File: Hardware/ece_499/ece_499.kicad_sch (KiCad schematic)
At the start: 64 parts, among them J1 Conn_01x04, J2 Conn_01x04, J3 Conn_01x04, J4 Conn_01x04, J5 Conn_01x04, Q1 DMN2004WK, Q2 DMN2004WK, Q3 DMN2004WK, Q4 DMN2004WK, SW1 Encoder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

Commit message: fix resistor values, update datasheet
-Fixed R1 values for debounce circuits
-Changed all 2.7k resistors to 3k
-Updated datasheet for DMN2004WK
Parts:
- R11, R13, R14, R15, R16, R3, R5: value 2.7k -> 3k
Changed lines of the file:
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@@
 			)
 		)
-		(property "Value" "2.7k"
+		(property "Value" "3k"
 			(at 19.05 102.235 90)
 			(effects
@@
 			)
 		)
-		(property "Value" "2.7k"
+		(property "Value" "3k"
 			(at 73.025 88.9 90)
 			(effects
@@
 			)
 		)
-		(property "Datasheet" "https://www.diodes.com/assets/Datasheets/ds30934.pdf"
+		(property "Datasheet" "https://www.diodes.com/assets/Datasheets/DMN2004WK.pdf"
 			(at 34.925 171.45 0)
 			(effects
@@
 			)
 		)
-		(property "Value" "2.7k"
+		(property "Value" "3k"
 			(at 97.79 182.8799 0)
 			(effects
@@
 			)
 		)
-		(property "Datasheet" "https://www.diodes.com/assets/Datasheets/ds30934.pdf"
+		(property "Datasheet" "https://www.diodes.com/assets/Datasheets/DMN2004WK.pdf"
 			(at 100.965 171.45 0)
 			(effects
@@
 			)
 		)
-		(property "Value" "2.7k"
+		(property "Value" "3k"
 			(at 30.48 182.8799 0)
 			(effects
@@
 			)
 		)
-		(property "Value" "2.7k"
+		(property "Value" "3k"
 			(at 64.77 182.8799 0)
 			(effects
@@
 			)
 		)
-		(property "Value" "2.7k"
+		(property "Value" "3k"
 			(at 18.415 88.9 90)
 			(effects
@@
 			)
 		)
-		(property "Datasheet" "https://www.diodes.com/assets/Datasheets/ds30934.pdf"
+		(property "Datasheet" "https://www.diodes.com/assets/Datasheets/DMN2004WK.pdf"
 			(at 133.985 171.45 0)
 			(effects
@@
 			)
 		)
-		(property "Datasheet" "https://www.diodes.com/assets/Datasheets/ds30934.pdf"
+		(property "Datasheet" "https://www.diodes.com/assets/Datasheets/DMN2004WK.pdf"
 			(at 67.945 171.45 0)
 			(effects
@@
 			)
 		)
-		(property "Value" "2.7k"
+		(property "Value" "3k"
 			(at 130.81 182.8799 0)
 			(effects

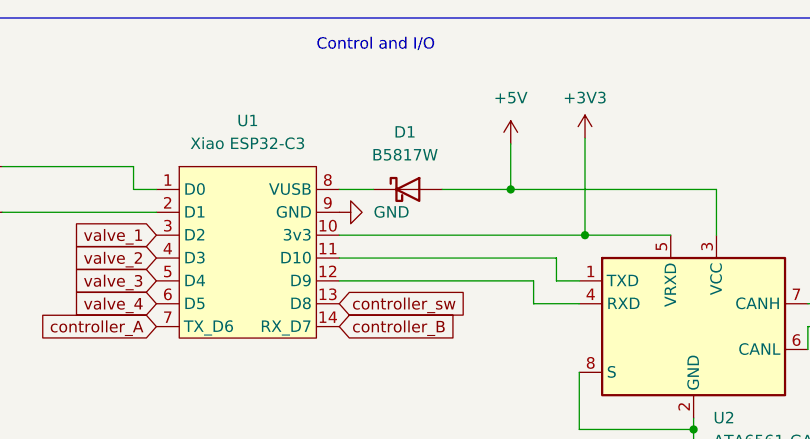
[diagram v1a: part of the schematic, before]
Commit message: Minor fixes     - Replace MCU diode with 1N5817     - Move 3v3 TP     - Remove 90 degree traces     - More stitching vias
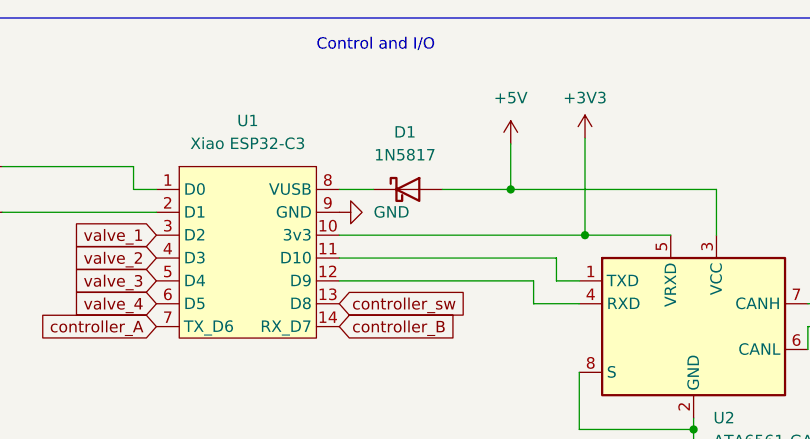
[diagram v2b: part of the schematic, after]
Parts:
- D1: value B5817W -> 1N5817; footprint Diode_SMD:D_SOD-123 -> Diode_THT:D_A-405_P7.62mm_Horizontal
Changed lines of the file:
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@@
 			)
 		)
-		(property "Value" "B5817W"
+		(property "Value" "1N5817"
 			(at 75.8825 27.94 0)
 			(effects
@@
 			)
 		)
-		(property "Footprint" "Diode_SMD:D_SOD-123"
+		(property "Footprint" "Diode_THT:D_A-405_P7.62mm_Horizontal"
 			(at 76.2 36.195 0)
 			(effects
